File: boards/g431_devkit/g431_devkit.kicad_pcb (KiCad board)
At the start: 2 copper layers, 41.8 x 24.2 mm, 18 parts, among them J1 usb_c_16p, J2 samtec_ftsh_107_01_l_dv_k, U1 ht7333, U2 VAL**

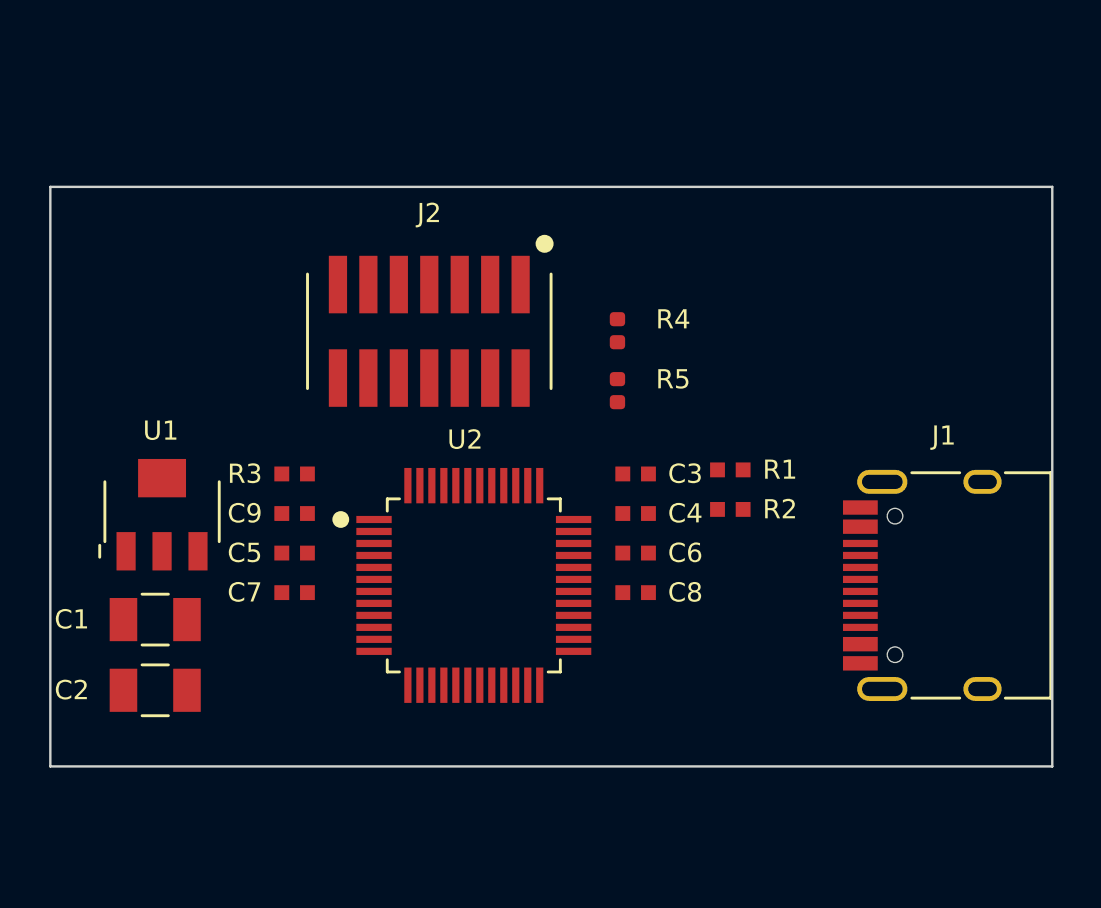
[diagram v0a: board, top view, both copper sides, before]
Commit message: P13: 블록 선언의 배치 지시 (place: role/near) — AI가 읽고 배치
- block.json parts[].place = {role, near}: g431_min의 디커플링 100nF 3개를
  각 VDD 핀(24/36/48), 벌크/VDDA/VREF+/NRST/BOOT0도 각 대상 핀에 선언.
- build_pcb: 지시를 ref_map으로 번역해 대상 핀 옆에 고정 배치 — 연결
  패드가 핀을 향하게 회전, 2차원(바깥+옆줄) 밀어내기로 변을 따라 나란히
  (바깥으로만 밀면 후보 소진 시 겹침 — C7/C8 사건).
- REF 배치 후보 탐색화: 옆/위/아래 중 안 겹치는 첫 자리 (U2 ref가 R3와
  충돌하던 것 해소). DRC 0.

Co-Authored-By: Claude Fable 5 <noreply@anthropic.com>
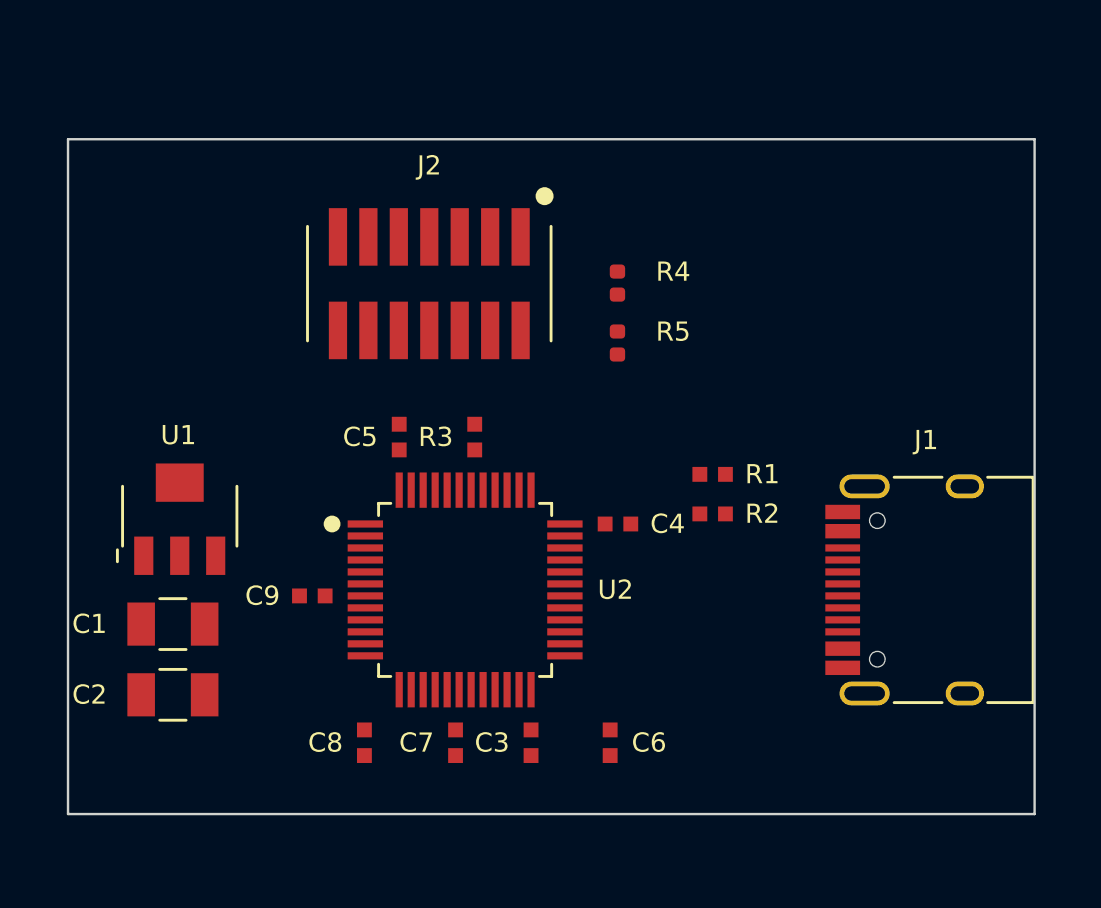
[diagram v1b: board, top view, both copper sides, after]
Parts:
- moved C8 12.9 mm to (140.7, 116.1), turned to 90 degrees
- moved C3 12.0 mm to (147.7, 116.1), turned to 90 degrees
- moved C7 9.18 mm to (144.5, 116.1), turned to 90 degrees
- moved C6 7.98 mm to (151.0, 116.1), turned to 90 degrees
- moved R3 7.67 mm to (145.3, 103.3), turned to 90 degrees
- moved C5 6.51 mm to (142.2, 103.3), turned to -90 degrees
- moved C9 3.52 mm to (138.5, 110.0)
- moved J2 1.99 mm to (143.4, 97.0)
- moved R4 1.99 mm to (151.3, 96.9)
- moved R5 1.99 mm to (151.3, 99.4)
- moved C4 0.86 mm to (151.3, 107.0), turned to 180 degrees
- moved C1 0.76 mm to (132.7, 111.1)
- moved C2 0.76 mm to (132.7, 114.1)
- moved J1 0.76 mm to (164.7, 109.7)
- moved U1 0.76 mm to (133.0, 106.7)
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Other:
- board size 41.8 x 24.2 mm -> 40.3 x 28.1 mm

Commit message: P14/P15: 전원 사슬 + 메인 IC 회전 선언 (U2 90도, 31x32mm)
- P15: board.json orient로 메인 IC 회전 — U2 90도로 SWD변이 왼쪽(J2 최좌),
  USB핀 변이 위(J1 위 가장자리). 회전 후 핀 변 재계산으로 군집·근접 캡 추종.
- P14: 전원 변환 군집(LDO)은 입력 전원 공급 군집(usb) 옆 — 블록 선언의
  깃발(공급)/power_in(소비) 사슬로 판단.
- 마감 정렬 재구성: 분리는 자기 변 접선 방향만(플러시 벽 진동 제거),
  가장자리 변은 벽 기준 밴드 정렬(깊은 군집만큼 벽 내림), 분리 판정은
  실겹침 0.6mm 기준(1.7mm 간격 오판으로 LDO 튕김 사건), 가장자리 군집
  내부 클램프는 일괄 이동, REF 폴백은 겹침 최소 후보.
- 근접 배치 패드 크기는 회전 반영 bbox로. DRC 0.

Co-Authored-By: Claude Fable 5 <noreply@anthropic.com>
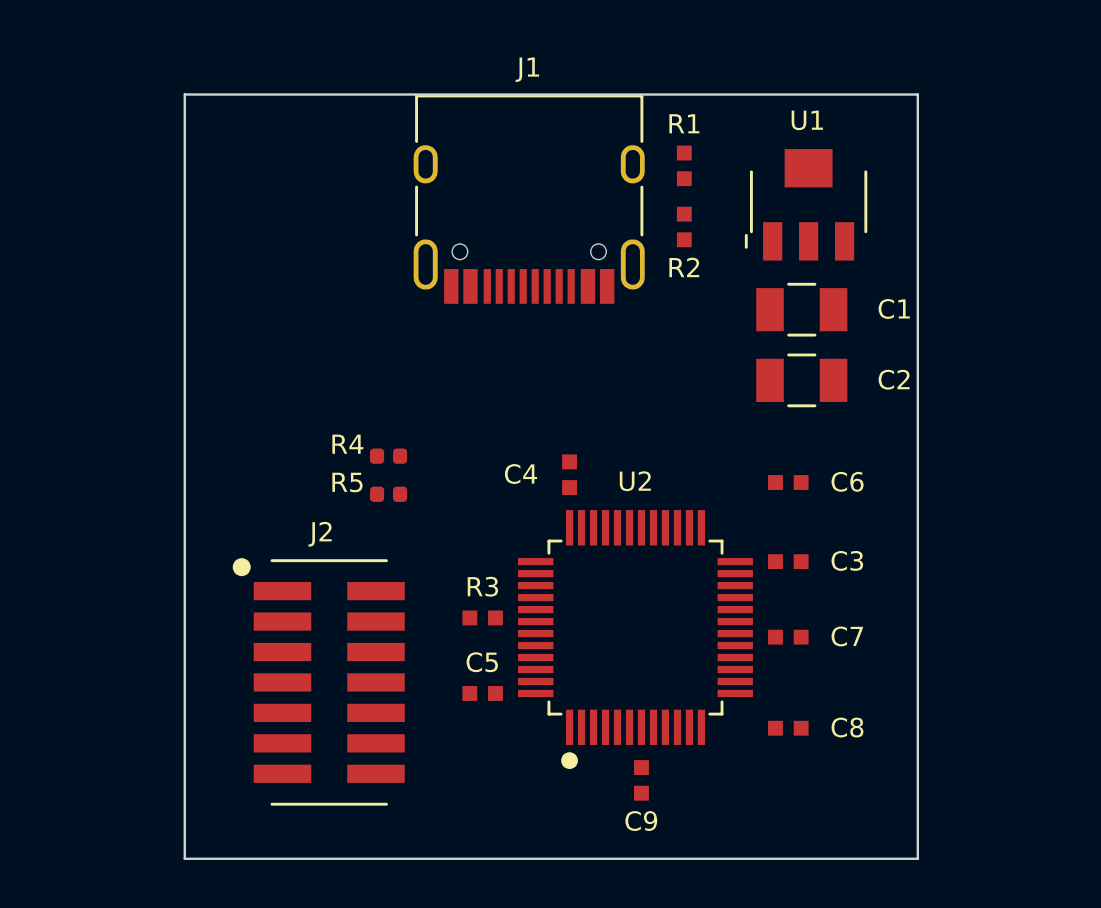
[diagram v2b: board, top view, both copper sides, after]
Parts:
- moved U1 29.3 mm to (159.2, 93.5)
- moved C2 29.3 mm to (158.9, 101.0)
- moved C1 29.3 mm to (158.9, 98.0)
- moved J1 23.9 mm to (147.6, 93.0), turned to 180 degrees
- moved C8 17.7 mm to (158.4, 115.5), turned to 180 degrees
- moved J2 17.2 mm to (139.2, 113.6), turned to -90 degrees
- moved C9 15.7 mm to (152.3, 117.7), turned to 90 degrees
- moved C7 14.6 mm to (158.4, 111.7), turned to 180 degrees
- moved C6 13.2 mm to (158.4, 105.2), turned to 180 degrees
- moved C3 13.1 mm to (158.4, 108.5), turned to 180 degrees
- moved R1 12.9 mm to (154.0, 92.0), turned to -90 degrees
- moved R2 12.0 mm to (154.0, 94.6), turned to -90 degrees
- moved R4 12.0 mm to (141.7, 104.1), turned to 180 degrees
- moved R5 11.4 mm to (141.7, 105.7), turned to 180 degrees
- moved C5 11.2 mm to (145.6, 114.0), turned to 0 degrees
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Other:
- board size 40.3 x 28.1 mm -> 30.6 x 31.9 mm
